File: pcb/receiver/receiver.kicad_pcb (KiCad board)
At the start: 2 copper layers, 200 parts, among them J101 Conn_01x02, J301 UART, J302 STM32_SWD, J303 AVR_DEBUG, J304 USB_B_Micro, Q101 BSS215PH6327XTSA1, Q102 MMBT2222A-7-F, Q201 BFR31,215, Q202 MMBT2222A-7-F, Q203 MMBT2222A-7-F, Q204 MMBT2222A-7-F, Q205 MMBT2222A-7-F, Q206 MMBT2222A-7-F, Q207 TF414T5G, U101 TPS63700DRCR, U102 NCP1403SNT1G, U201 ADR550ARTZ-REEL7, U202 TL974IPWR, U203 MAX4477AUA+, U204 OPA2141AIDR, U205 NLAS4599DFT2G, U301 ATTINY412-SSNR, U302 STM32F070F6P6, U303 MAX11666AUB+T, U304 L78L33ABUTR, Y301 ABM3B-8.000MHZ-10-1UT

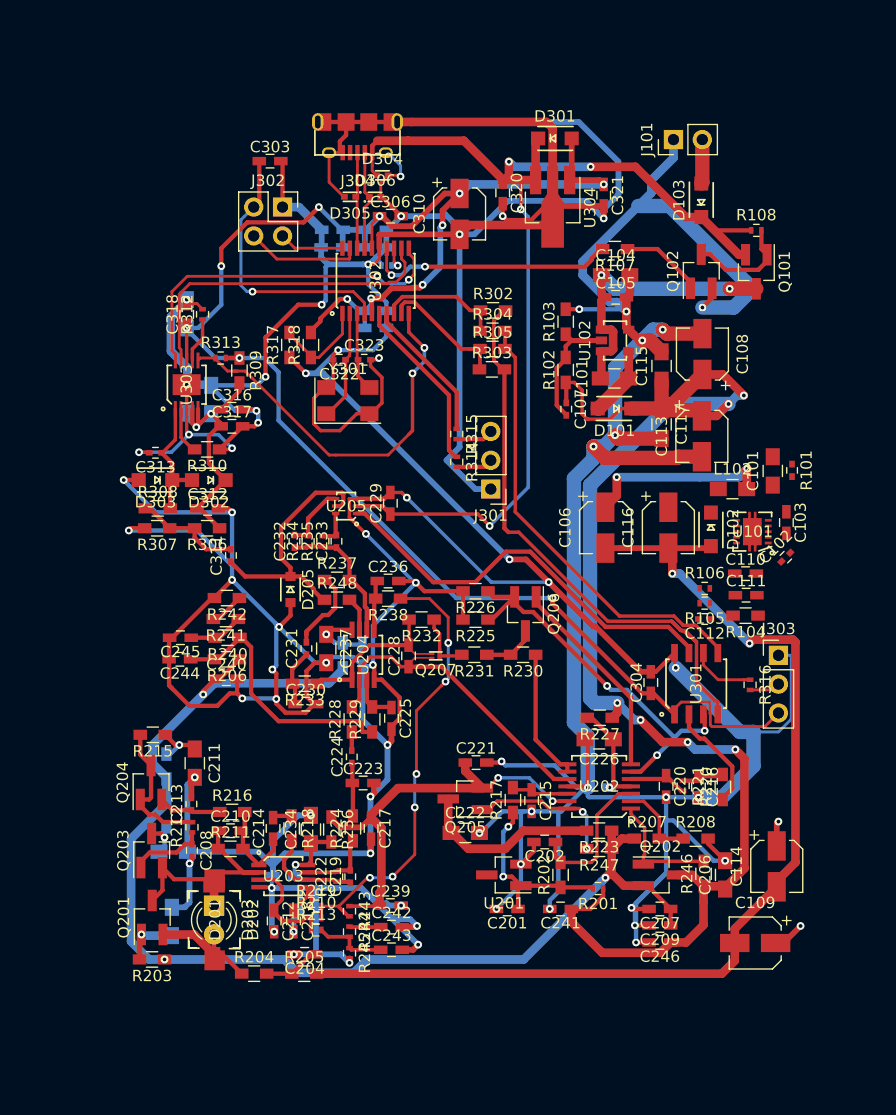
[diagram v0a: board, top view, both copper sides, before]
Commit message: Add copper fills and outline, autofill test point footprints, TODO finish placing test points and moving silkscreen
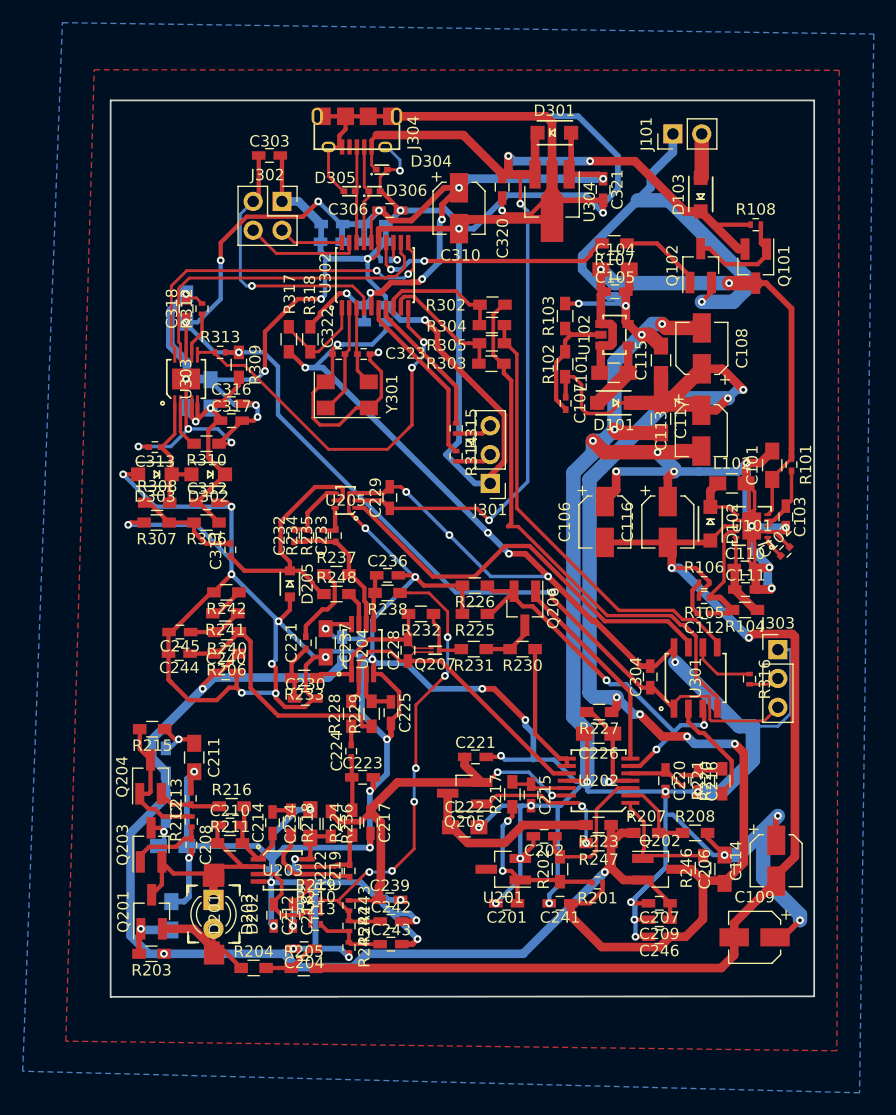
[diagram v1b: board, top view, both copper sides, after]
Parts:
- moved R311 0.50 mm to (51.9, 127.8)
- moved C102 0.50 mm to (87.1, 153.5)
- moved C104 0.50 mm to (72.1, 128.7)
- moved C105 0.50 mm to (72.1, 130.6)
- moved C111 0.50 mm to (83.6, 156.8)
- moved C202 0.50 mm to (65.8, 178.6)
- moved C227 0.50 mm to (70.6, 173.8)
- moved R207 0.50 mm to (74.8, 178.3)
- moved R246 0.50 mm to (79.8, 181.4)
- moved C201 0.50 mm to (62.5, 184.5)
- moved C210 0.50 mm to (38.2, 177.6)
- moved C214 0.50 mm to (41.9, 177.4)
- moved C217 0.50 mm to (50.5, 177.4)
- moved C221 0.50 mm to (59.8, 171.6)
- moved C232 0.50 mm to (43.8, 152.1)
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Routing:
- net GND: track 827.8 -> 933.7 mm, vias 72 -> 83
- net /+5V: track 25.4 -> 48.5 mm
- net Net-(C112-Pad1): track 0.00 -> 11.7 mm
- net -12V: track 93.0 -> 101.3 mm
- net Net-(C103-Pad1): track 0.00 -> 7.99 mm
- net Net-(C110-Pad1): track 0.00 -> 7.43 mm
- net Net-(D102-Pad1): track 0.00 -> 4.87 mm
- net Net-(C112-Pad2): track 0.00 -> 3.17 mm
- net Net-(C102-Pad1): track 0.00 -> 2.12 mm
- net /Photodiode/+2V5: track 42.3 -> 43.2 mm
- added copper zone on B.Cu, net GND
- added copper zone on F.Cu, net GND
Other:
- board outline added: 62 x 79 mm

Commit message: Finish silkscreen stuff
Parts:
- added TP101: TestPoint, Measurement_Points:Measurement_Point_Round-SMD-Pad_Small, F.Cu at (87.1, 173.6)
- added TP102: TestPoint, Measurement_Points:Measurement_Point_Round-SMD-Pad_Small, F.Cu at (84.0, 173.1)
- added TP201: TestPoint, Measurement_Points:Measurement_Point_Round-SMD-Pad_Small, F.Cu at (45.2, 169.8)
- added TP202: TestPoint, Measurement_Points:Measurement_Point_Round-SMD-Pad_Small, B.Cu at (49.9, 187.2)
- added TP204: TestPoint, Measurement_Points:Measurement_Point_Round-SMD-Pad_Small, F.Cu at (54.7, 172.2)
- added TP205: TestPoint, Measurement_Points:Measurement_Point_Round-SMD-Pad_Small, F.Cu at (41.8, 169.4)
- added TP206: TestPoint, Measurement_Points:Measurement_Point_Round-SMD-Pad_Small, F.Cu at (39.5, 173.9)
- added TP207: TestPoint, Measurement_Points:Measurement_Point_Round-SMD-Pad_Small, B.Cu at (47.8, 181.1)
- added TP208: TestPoint, Measurement_Points:Measurement_Point_Round-SMD-Pad_Small, B.Cu at (53.6, 159.5)
- added TP209: TestPoint, Measurement_Points:Measurement_Point_Round-SMD-Pad_Small, F.Cu at (40.1, 153.7)
- added TP301: TestPoint, Measurement_Points:Measurement_Point_Round-SMD-Pad_Small, F.Cu at (75.1, 120.4)
- added TP302: TestPoint, Measurement_Points:Measurement_Point_Round-SMD-Pad_Small, F.Cu at (82.9, 167.1)
- added TP303: TestPoint, Measurement_Points:Measurement_Point_Round-SMD-Pad_Small, F.Cu at (83.0, 163.0)
- added TP304: TestPoint, Measurement_Points:Measurement_Point_Round-SMD-Pad_Small, F.Cu at (36.8, 125.8)
- R302, R305: value 0 -> 0 DNP
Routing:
- net /Photodiode/+1V0: track 6.54 -> 12.3 mm, vias 0 -> 1
- net /Digital/ATTINY_RXD: track 39.7 -> 42.1 mm
- net Net-(C210-Pad2): track 8.23 -> 10.3 mm
- net +12V: track 123.9 -> 126.0 mm
- net /Digital/ATTINY_TXD: track 51.7 -> 53.5 mm
- net /Photodiode/+7V5: track 23.0 -> 24.9 mm
- net /Digital/+3V3: track 163.0 -> 164.7 mm
- net /Digital/ADC_AIN: track 22.8 -> 24.4 mm
- net Net-(C219-Pad2): track 6.52 -> 7.70 mm, vias 0 -> 1
- net -12V: track 101.3 -> 102.3 mm
- net Net-(C228-Pad2): track 15.1 -> 15.8 mm, vias 0 -> 1
- net GND: track 933.7 -> 934.3 mm
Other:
- board text added: "Photodiode receiver Rev. 1"
